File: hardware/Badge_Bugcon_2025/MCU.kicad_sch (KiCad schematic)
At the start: 58 parts, among them J1 Flash, J2 Conn_01x04_Pin, SW2 SW_Push, SW3 SW_Push, U6 W25N02KVZEIR, Y1 Crystal, Y2 24MHz

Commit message: feat(Hw):Update_Schematic
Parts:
- added J11, J12, J13, J14, J15: Conn_01x11, Connector_PinHeader_2.54mm:PinHeader_1x11_P2.54mm_Vertical, symbol Connector_Generic:Conn_01x11
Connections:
- net CODEC_LINEOUT: now also J11.9 (Pin_9)
- net CODEC_MIC0N: now also J11.11 (Pin_11)
- net CODEC_MIC0P: now also J12.1 (Pin_1)
- net CODEC_MIC1N: now also J12.2 (Pin_2)
- net CODEC_MIC1P: now also J12.3 (Pin_3)
- net CODEC_MICBIAS: now also J11.10 (Pin_10)
- net ETH_EXTR: now also J14.6 (Pin_6)
- net ETH_PHY_RXN: now also J14.1 (Pin_1)
- net ETH_PHY_RXP: now also J14.2 (Pin_2)
- net ETH_PHY_TXN: now also J14.3 (Pin_3)
- net ETH_PHY_TXP: now also J14.4 (Pin_4)
- net GPIO0_A0_Z: now also J12.8 (Pin_8)
- net GPIO0_A1_D: now also J12.9 (Pin_9)
- net GPIO0_A3_U: now also J12.10 (Pin_10)
- net GPIO0_A4_D: now also J12.11 (Pin_11)
- net GPIO1_B0_D: now also J13.1 (Pin_1)
- net GPIO1_C0_D: now also J14.5 (Pin_5)
- net GPIO1_C1_D: now also J13.11 (Pin_11)
- net GPIO1_C3_D: now also J13.10 (Pin_10)
- net GPIO1_C4_D: now also J13.9 (Pin_9)
- net GPIO1_C5_D: now also J13.8 (Pin_8)
- net GPIO1_C6_D: now also J13.2 (Pin_2)
- net GPIO1_C7_D: now also J13.3 (Pin_3)
- net GPIO1_D0_D: now also J13.7 (Pin_7)
- net GPIO1_D1_D: now also J13.6 (Pin_6)
- net GPIO1_D2_D: now also J13.5 (Pin_5)
- net GPIO1_D3_D: now also J13.4 (Pin_4)
- net GPIO2_A0_D_1: now also J14.11 (Pin_11)
- net GPIO2_A0_D_2: now also J15.1 (Pin_1)
- net GPIO2_A3_D: now also J15.3 (Pin_3)
- net GPIO2_A4_D: now also J15.4 (Pin_4)
- net GPIO2_A5_D: now also J15.5 (Pin_5)
- net GPIO2_A6_D: now also J14.10 (Pin_10)
- net GPIO2_A7_D: now also J14.9 (Pin_9)
- net GPIO2_A_2_D: now also J15.2 (Pin_2)
- net GPIO2_B1_D_1: now also J14.7 (Pin_7)
- net GPIO2_B1_D_2: now also J14.8 (Pin_8)
- net GPIO3_B2_D: now also J15.6 (Pin_6)
- net GPIO3_B3_D: now also J15.7 (Pin_7)
- net GPIO3_C0_D: now also J15.8 (Pin_8)
- net GPIO3_C1_D: now also J15.9 (Pin_9)
- net GPIO3_C2_D: now also J15.10 (Pin_10)
- net GPIO3_C3_D: now also J15.11 (Pin_11)
- net GPIO3_C4_D: now also J11.1 (Pin_1)
- net GPIO3_C5_D: now also J11.2 (Pin_2)
- net GPIO3_C7_D: now also J11.3 (Pin_3)
- net GPIO3_D0_D: now also J11.5 (Pin_5)
- net GPIO3_D1_D: now also J11.4 (Pin_4)
- net GPIO3_D2_D: now also J11.6 (Pin_6)
- net GPIO3_D3_D: now also J11.7 (Pin_7)
- net GPIO4_A0_U: now also J12.7 (Pin_7)
- net GPIO4_A1_U: now also J12.6 (Pin_6)
- net GPIO4_A5_U: now also J12.5 (Pin_5)
- net GPIO4_A7_U: now also J12.4 (Pin_4)
- net GPIO4_C1_Z: now also J11.8 (Pin_8)
- net GPIO3_B4_D renamed LEFT
- net GPIO3_B5_D renamed RIGHT
- net GPIO3_B6_D renamed DOWN
- net GPIO3_B7_D renamed UP
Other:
- note added: "PINES"
- moved on the sheet: C51, C52, J1, J2, R28, R35, R36, U6

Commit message: feat(Hw):Update_Schematic
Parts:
- removed J11, J12, J13, J14, J15: Conn_01x11, Connector_PinHeader_2.54mm:PinHeader_1x11_P2.54mm_Vertical, symbol Connector_Generic:Conn_01x11
- added J11: +1V8, symbol Connector_Generic:Conn_01x30
- added J12: CODEC, symbol Connector_Generic:Conn_01x08
- added J13: ETH, symbol Connector_Generic:Conn_01x07
- added J14: +3V3, symbol Connector_Generic:Conn_01x28
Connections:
- net GPIO0_A0_Z is gone; now on net LEFT: U8.58 (UART0_RX_M0/CLK_32K/CLK_REFOUT/RTC_CLKO/GPIO0_A0_Z)
- net GPIO0_A1_D is gone; now on net RIGHT: U8.59 (UART0_TX_M0/PWM2_M0/GPIO0_A1_D)
- net GPIO0_A3_U is gone; now on net DOWN: U8.62 (PMIC_PWR_CTRL_M1/GPIO0_A3_U)
- net GPIO0_A4_D is gone; now on net UP: U8.63 (PMIC_PWR_CTRL_M0/PWM1_M0/GPIO0_A4_D)
- net +1V8: now also J11.1 (Pin_1)
- net +3V3: now also J14.1 (Pin_1)
- net CODEC_LINEOUT: now also J12.2 (Pin_2)
- net CODEC_MIC0N: now also J12.4 (Pin_4)
- net CODEC_MIC0P: now also J12.5 (Pin_5)
- net CODEC_MIC1N: now also J12.6 (Pin_6)
- net CODEC_MIC1P: now also J12.7 (Pin_7)
- net CODEC_MICBIAS: now also J12.3 (Pin_3)
- net DOWN: no longer U8.123 (VI_CIF_D6_M0/MIPI_CSI_RX_D1N/LVDS_RX_D1N/GPIO_3_B6_D)
- net ETH_EXTR: now also J13.6 (Pin_6)
- net ETH_PHY_RXN: now also J13.2 (Pin_2)
- net ETH_PHY_RXP: now also J13.3 (Pin_3)
- net ETH_PHY_TXN: now also J13.4 (Pin_4)
- net ETH_PHY_TXP: now also J13.5 (Pin_5)
- net GND: now also J11.30 (Pin_30), J12.8 (Pin_8), J13.7 (Pin_7), J14.28 (Pin_28)
- net GPIO1_B0_D: now also J14.6 (Pin_6)
- net GPIO1_C0_D: now also J14.17 (Pin_17)
- net GPIO1_C1_D: now also J14.16 (Pin_16)
- net GPIO1_C3_D: now also J14.15 (Pin_15)
- net GPIO1_C4_D: now also J14.14 (Pin_14)
- net GPIO1_C5_D: now also J14.13 (Pin_13)
- net GPIO1_C6_D: now also J14.7 (Pin_7)
- net GPIO1_C7_D: now also J14.8 (Pin_8)
- net GPIO1_D0_D: now also J14.12 (Pin_12)
- net GPIO1_D1_D: now also J14.11 (Pin_11)
- net GPIO1_D2_D: now also J14.10 (Pin_10)
- net GPIO1_D3_D: now also J14.9 (Pin_9)
- net GPIO2_A0_D_1: now also J14.22 (Pin_22)
- net GPIO2_A0_D_2: now also J14.23 (Pin_23)
- net GPIO2_A3_D: now also J14.25 (Pin_25)
- net GPIO2_A4_D: now also J14.26 (Pin_26)
- net GPIO2_A5_D: now also J14.27 (Pin_27)
- net GPIO2_A6_D: now also J14.21 (Pin_21)
- net GPIO2_A7_D: now also J14.20 (Pin_20)
- net GPIO2_A_2_D: now also J14.24 (Pin_24)
- net GPIO2_B1_D_1: now also J14.18 (Pin_18)
- net GPIO2_B1_D_2: now also J14.19 (Pin_19)
- net GPIO3_B2_D: now also J11.20 (Pin_20), J11.9 (Pin_9)
- net GPIO3_B3_D: now also J11.10 (Pin_10), J11.21 (Pin_21)
- net GPIO3_C0_D: now also J11.15 (Pin_15), J11.26 (Pin_26)
- net GPIO3_C1_D: now also J11.16 (Pin_16), J11.27 (Pin_27)
- net GPIO3_C2_D: now also J11.17 (Pin_17), J11.28 (Pin_28)
- net GPIO3_C3_D: now also J11.18 (Pin_18), J11.29 (Pin_29)
- net GPIO3_C4_D: now also J11.2 (Pin_2)
- net GPIO3_C5_D: now also J11.3 (Pin_3)
- net GPIO3_C7_D: now also J11.4 (Pin_4)
- net GPIO3_D0_D: now also J11.6 (Pin_6)
- net GPIO3_D1_D: now also J11.5 (Pin_5)
- net GPIO3_D2_D: now also J11.7 (Pin_7)
- net GPIO3_D3_D: now also J11.8 (Pin_8)
- net GPIO4_A0_U: now also J14.5 (Pin_5)
- net GPIO4_A1_U: now also J14.4 (Pin_4)
- net GPIO4_A5_U: now also J14.3 (Pin_3)
- net GPIO4_A7_U: now also J14.2 (Pin_2)
- net GPIO4_C1_Z: now also J11.19 (Pin_19)
- net LEFT: no longer U8.121 (VI_CIF_D4_M0/MIPI_CSI_RX_D2N/LVDS_RX_D2N/GPIO_3_B4_D)
- net RIGHT: no longer U8.122 (VI_CIF_D5_M0/MIPI_CSI_RX_D2P/LVDS_RX_D2P/GPIO3__B5_D)
- net UP: no longer U8.124 (VI_CIF_D7_M0/MIPI_CSI_RX_D1P/LVDS_RX_D1P/GPIO3__B7_D)
- net VCC1V8_CODEC: now also J12.1 (Pin_1)
- net ETH_AVDD3V3: now reaches R29.2, U8.101 (ETH_AVDD3V3)
- net ETH_AVDD3V3: now also J13.1 (Pin_1)
- new net GPIO3_B4_D: J11.11 (Pin_11), J11.22 (Pin_22), U8.121 (VI_CIF_D4_M0/MIPI_CSI_RX_D2N/LVDS_RX_D2N/GPIO_3_B4_D)
- new net GPIO3_B5_D: J11.12 (Pin_12), J11.23 (Pin_23), U8.122 (VI_CIF_D5_M0/MIPI_CSI_RX_D2P/LVDS_RX_D2P/GPIO3__B5_D)
- new net GPIO3_B6_D: J11.13 (Pin_13), J11.24 (Pin_24), U8.123 (VI_CIF_D6_M0/MIPI_CSI_RX_D1N/LVDS_RX_D1N/GPIO_3_B6_D)
- new net GPIO3_B7_D: J11.14 (Pin_14), J11.25 (Pin_25), U8.124 (VI_CIF_D7_M0/MIPI_CSI_RX_D1P/LVDS_RX_D1P/GPIO3__B7_D)
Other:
- moved on the sheet: C1, C20, C23, C24, C25, C26, C27, C28, C29, C3, C30, C34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

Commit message: feat(Hw):Update_Schematic
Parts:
- removed J11: +1V8, symbol Connector_Generic:Conn_01x30
- added J11: Conn_01x20, symbol Connector_Generic:Conn_01x20
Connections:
- net +1V8: now also J11.1 (Pin_1)
- net GND: now also J11.20 (Pin_20)
- net GPIO3_B2_D: now also J11.9 (Pin_9)
- net GPIO3_B3_D: now also J11.10 (Pin_10)
- net GPIO3_B4_D: now also J11.11 (Pin_11)
- net GPIO3_B5_D: now also J11.12 (Pin_12)
- net GPIO3_B6_D: now also J11.13 (Pin_13)
- net GPIO3_B7_D: now also J11.14 (Pin_14)
- net GPIO3_C0_D: now also J11.15 (Pin_15)
- net GPIO3_C1_D: now also J11.16 (Pin_16)
- net GPIO3_C2_D: now also J11.17 (Pin_17)
- net GPIO3_C3_D: now also J11.18 (Pin_18)
- net GPIO3_C4_D: now also J11.2 (Pin_2)
- net GPIO3_C5_D: now also J11.3 (Pin_3)
- net GPIO3_C7_D: now also J11.4 (Pin_4)
- net GPIO3_D0_D: now also J11.6 (Pin_6)
- net GPIO3_D1_D: now also J11.5 (Pin_5)
- net GPIO3_D2_D: now also J11.7 (Pin_7)
- net GPIO3_D3_D: now also J11.8 (Pin_8)
- net GPIO4_C1_Z: now also J11.19 (Pin_19)

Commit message: feat(Hw):Update_BOM
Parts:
- R28: LCSC# (none) -> C106231
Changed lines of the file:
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@@
+			)
+		)
+		(property "LCSC#" "C106231"
+			(at 95.25 176.53 90)
+			(effects
+				(font
+					(size 1.27 1.27)
+				)
+				(hide yes)
 			)
 		)

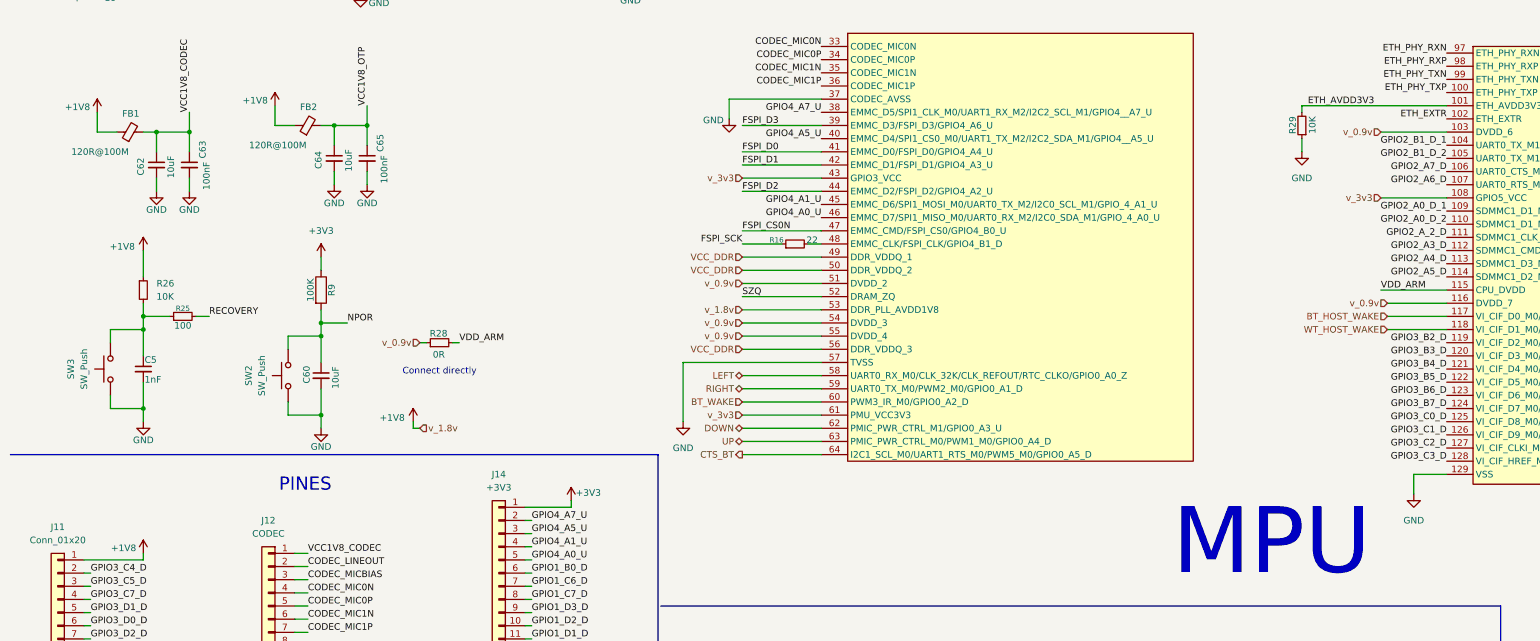
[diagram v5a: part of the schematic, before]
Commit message: feat(Hw):Update_Schematic_And_Floorplan
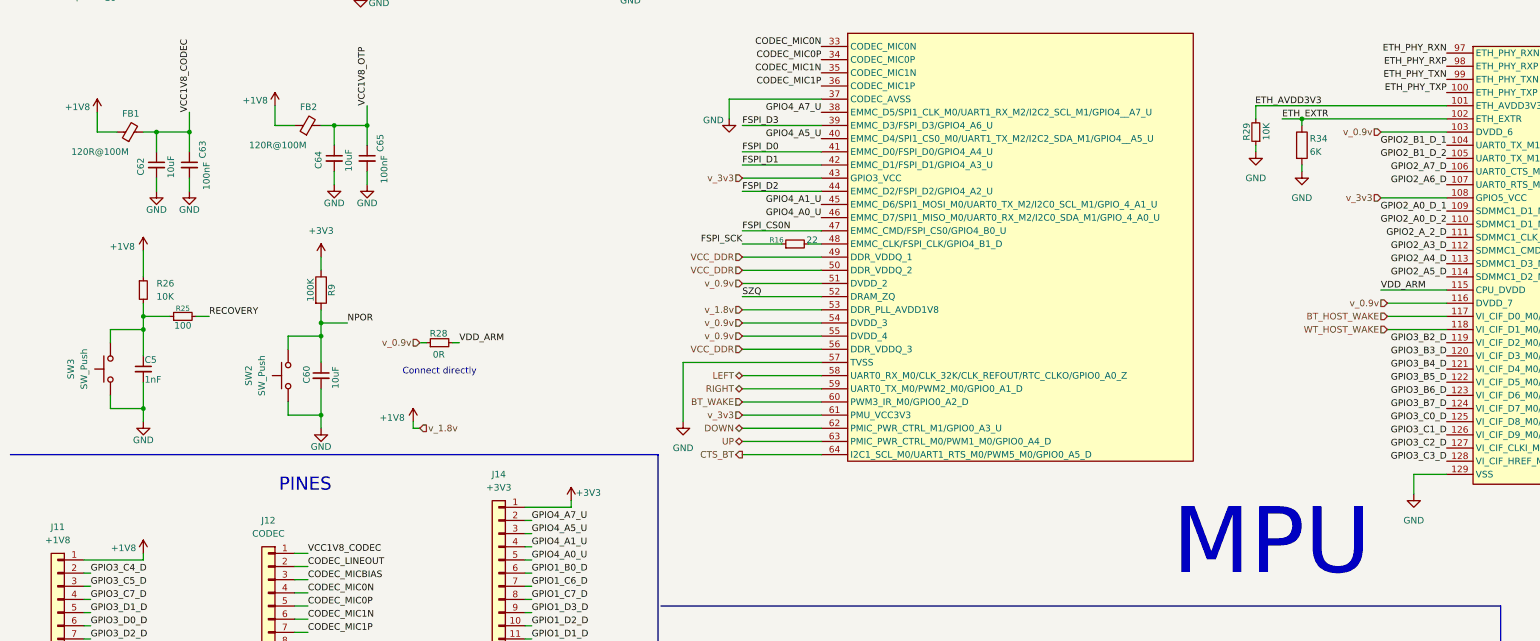
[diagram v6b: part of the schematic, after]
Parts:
- added R34: 6K, symbol Device:R
- C1: footprint Capacitor_SMD:C_0603_1608Metric -> Capacitor_SMD:C_0402_1005Metric; LCSC# C162274 -> C6119795
- C24, C28, C34, C38, C48, C51, C62, C64: footprint Capacitor_SMD:C_0603_1608Metric -> Capacitor_SMD:C_0402_1005Metric; LCSC# C96446 -> C7472949
- J11: value Conn_01x20 -> +1V8; footprint (none) -> Connector_PinHeader_2.54mm:PinHeader_1x20_P2.54mm_Vertical
- J12: footprint (none) -> Connector_PinHeader_2.54mm:PinHeader_1x08_P2.54mm_Vertical
- J13: footprint (none) -> Connector_PinHeader_2.54mm:PinHeader_1x07_P2.54mm_Vertical
- J14: footprint (none) -> Connector_PinHeader_2.54mm:PinHeader_1x28_P2.54mm_Vertical
- R16, R17: footprint Resistor_SMD:R_0603_1608Metric -> Resistor_SMD:R_0402_1005Metric; LCSC# (none) -> C159964; manf# SG73P1JTTD22R0F -> (none)
- R25, R27, R3: footprint Resistor_SMD:R_0603_1608Metric -> Resistor_SMD:R_0402_1005Metric; LCSC# C253328 -> C2906860
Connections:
- net ETH_EXTR: now also R34.1
- net GND: now also R34.2
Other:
- moved on the sheet: R29

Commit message: feat(Hw):Update_Schematic
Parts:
- removed J11: +1V8, Connector_PinHeader_2.54mm:PinHeader_1x20_P2.54mm_Vertical, symbol Connector_Generic:Conn_01x20
- removed J2: Conn_01x04_Pin, Connector_PinHeader_2.54mm:PinHeader_1x04_P2.54mm_Vertical, symbol Connector:Conn_01x04_Pin
- added J11: +1V8, Connector_PinHeader_2.54mm:PinHeader_1x28_P2.54mm_Vertical, symbol Connector_Generic:Conn_01x21
- added J2: Conn_01x04, Connector_PinHeader_2.54mm:PinHeader_1x04_P2.54mm_Vertical, symbol Connector_Generic:Conn_01x04
- J1, J12: manf# (none) -> 87220-8
- J13: manf# (none) -> 87224-7
- J14: manf# (none) -> 9-146278-0
- R34: footprint (none) -> Resistor_SMD:R_0805_2012Metric; LCSC# (none) -> C2828725
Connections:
- net +1V8: now also J11.1 (Pin_1)
- net +3V3: now also J2.1 (Pin_1)
- net DEBUG_RX: now also J2.3 (Pin_3)
- net DEBUG_TX: now also J2.2 (Pin_2)
- net GND: now also J11.21 (Pin_21), J2.4 (Pin_4)
- net GPIO3_B2_D: now also J11.10 (Pin_10)
- net GPIO3_B3_D: now also J11.11 (Pin_11)
- net GPIO3_B4_D: now also J11.12 (Pin_12)
- net GPIO3_B5_D: now also J11.13 (Pin_13)
- net GPIO3_B6_D: now also J11.14 (Pin_14)
- net GPIO3_B7_D: now also J11.15 (Pin_15)
- net GPIO3_C0_D: now also J11.16 (Pin_16)
- net GPIO3_C1_D: now also J11.17 (Pin_17)
- net GPIO3_C2_D: now also J11.18 (Pin_18)
- net GPIO3_C3_D: now also J11.19 (Pin_19)
- net GPIO3_C4_D: now also J11.2 (Pin_2)
- net GPIO3_C5_D: now also J11.3 (Pin_3)
- net GPIO3_C7_D: now also J11.5 (Pin_5)
- net GPIO3_D0_D: now also J11.7 (Pin_7)
- net GPIO3_D1_D: now also J11.6 (Pin_6)
- net GPIO3_D2_D: now also J11.8 (Pin_8)
- net GPIO3_D3_D: now also J11.9 (Pin_9)
- net GPIO4_C1_Z: now also J11.20 (Pin_20)
- net LED: now also J11.4 (Pin_4)
